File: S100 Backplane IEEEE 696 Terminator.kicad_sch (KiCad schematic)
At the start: 30 parts, among them IC1 7805, IC2 LM4250, P2 BUS_IN_1, P3 BUS_IN_2, Q1 2N3906, Q2 2N3904, Q3 TIP29, Q4 TIP30

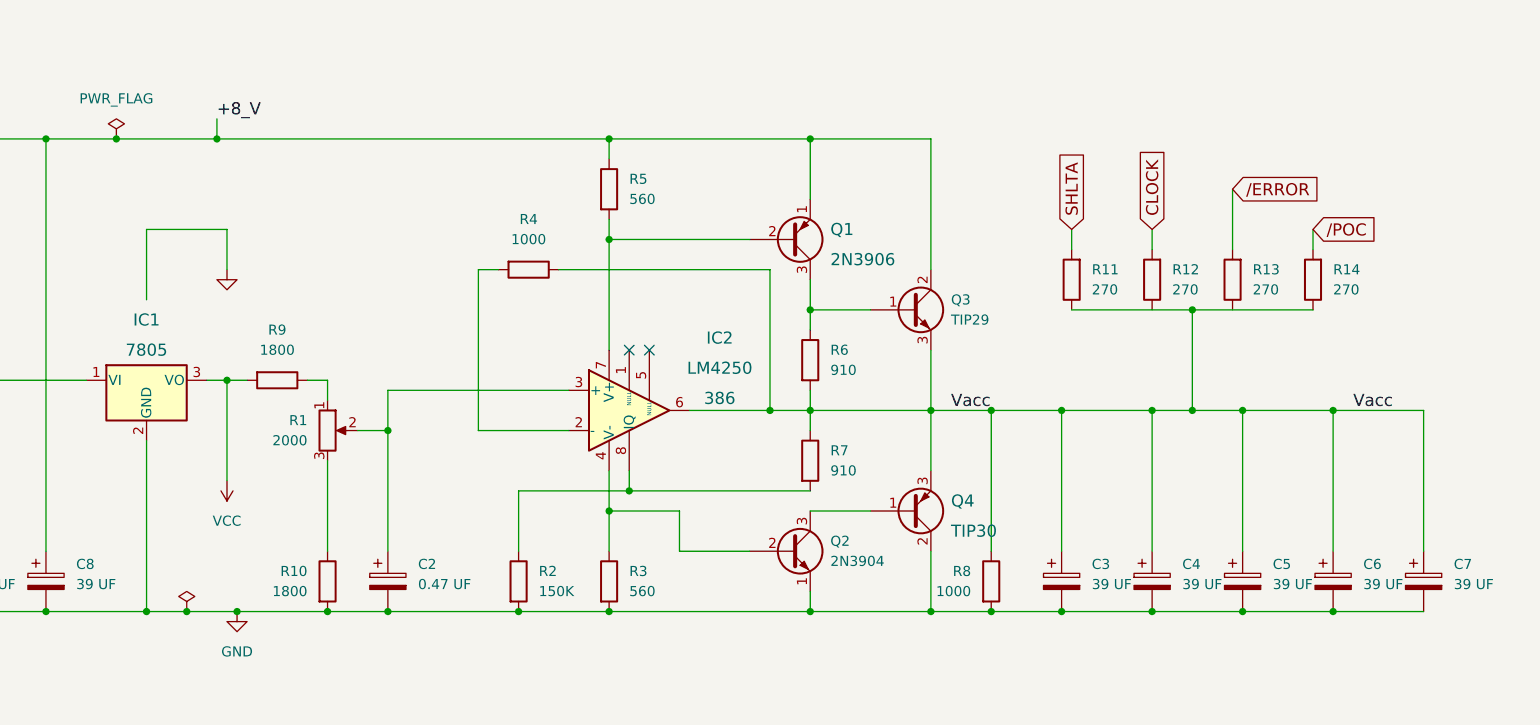
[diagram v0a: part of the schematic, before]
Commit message: Fix minor problem.
Signed-off-by: John Bradley <flypie@rocketmail.com>
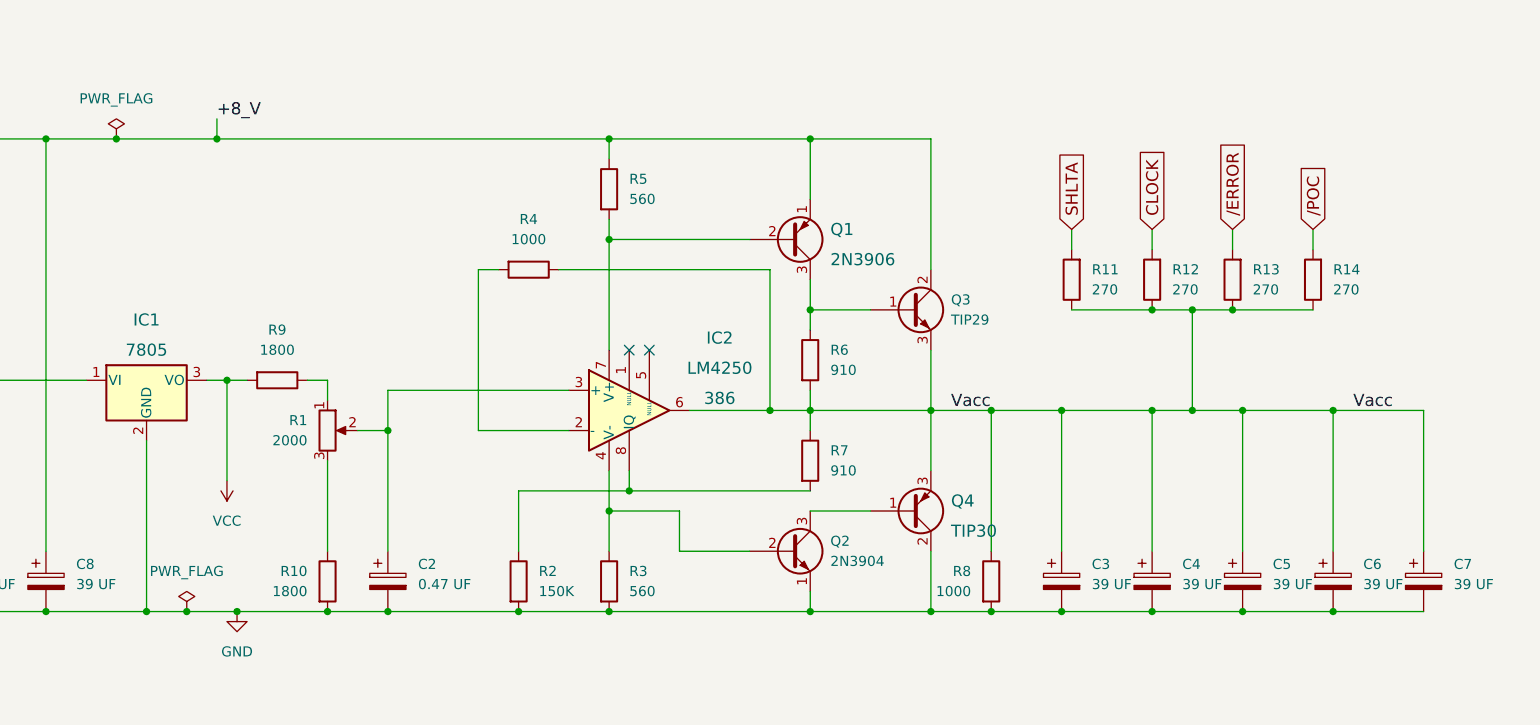
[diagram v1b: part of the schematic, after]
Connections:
- net Vacc: now also R12.1, R13.1
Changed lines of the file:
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@@
   (junction (at 226.06 92.71) (diameter 0) (color 0 0 0 0)
   )
+  (junction (at 237.49 54.61) (diameter 0) (color 0 0 0 0)
+  )
   (junction (at 194.31 33.02) (diameter 0) (color 0 0 0 0)
   )
@@
   )
   (junction (at 171.45 77.47) (diameter 0) (color 0 0 0 0)
+  )
+  (junction (at 247.65 54.61) (diameter 0) (color 0 0 0 0)
   )
   (junction (at 217.17 67.31) (diameter 0) (color 0 0 0 0)
@@
     (stroke (width 0) (type default) (color 0 0 0 0))
   )
-  (wire (pts (xy 110.49 53.34) (xy 110.49 44.45))
-    (stroke (width 0) (type default) (color 0 0 0 0))
-  )
   (wire (pts (xy 33.02 138.43) (xy 35.56 138.43))
     (stroke (width 0) (type default) (color 0 0 0 0))
@@
     (stroke (width 0) (type default) (color 0 0 0 0))
   )
-  (wire (pts (xy 120.65 44.45) (xy 120.65 49.53))
-    (stroke (width 0) (type default) (color 0 0 0 0))
-  )
   (wire (pts (xy 133.35 63.5) (xy 133.35 66.04))
     (stroke (width 0) (type default) (color 0 0 0 0))
@@
     (stroke (width 0) (type default) (color 0 0 0 0))
   )
-  (wire (pts (xy 227.33 54.61) (xy 242.57 54.61))
+  (wire (pts (xy 227.33 54.61) (xy 237.49 54.61))
     (stroke (width 0) (type default) (color 0 0 0 0))
   )
@@
     (stroke (width 0) (type default) (color 0 0 0 0))
   )
-  (wire (pts (xy 247.65 46.99) (xy 247.65 39.37))
+  (wire (pts (xy 247.65 46.99) (xy 247.65 44.45))
     (stroke (width 0) (type default) (color 0 0 0 0))
   )
@@
     (stroke (width 0) (type default) (color 0 0 0 0))
   )
-  (wire (pts (xy 110.49 44.45) (xy 120.65 44.45))
-    (stroke (width 0) (type default) (color 0 0 0 0))
-  )
   (wire (pts (xy 217.17 92.71) (xy 226.06 92.71))
     (stroke (width 0) (type default) (color 0 0 0 0))
@@
     (stroke (width 0) (type default) (color 0 0 0 0))
   )
-  (wire (pts (xy 242.57 54.61) (xy 257.81 54.61))
+  (wire (pts (xy 242.57 54.61) (xy 247.65 54.61))
+    (stroke (width 0) (type default) (color 0 0 0 0))
+  )
+  (wire (pts (xy 247.65 54.61) (xy 257.81 54.61))
     (stroke (width 0) (type default) (color 0 0 0 0))
   )
@@
   )
   (wire (pts (xy 48.26 57.15) (xy 50.8 57.15))
+    (stroke (width 0) (type default) (color 0 0 0 0))
+  )
+  (wire (pts (xy 237.49 54.61) (xy 242.57 54.61))
     (stroke (width 0) (type default) (color 0 0 0 0))
   )
@@
     )
   )
-  (global_label "/POC" (shape input) (at 257.81 44.45 0) (fields_autoplaced)
-    (effects (font (size 1.524 1.524)) (justify left))
-    (property "Intersheet References" "${INTERSHEET_REFS}" (id 0) (at 266.84 44.3548 0)
+  (global_label "/POC" (shape input) (at 257.81 44.45 90) (fields_autoplaced)
+    (effects (font (size 1.524 1.524)) (justify left))
+    (property "Intersheet References" "${INTERSHEET_REFS}" (id 0) (at 257.7148 35.42 90)
       (effects (font (size 1.524 1.524)) (justify left))
     )
@@
     )
   )
-  (global_label "{slash}ERROR" (shape input) (at 247.65 39.37 0) (fields_autoplaced)
-    (effects (font (size 1.524 1.524)) (justify left))
-    (property "Intersheet References" "${INTERSHEET_REFS}" (id 0) (at 259.5829 39.2748 0)
+  (global_label "{slash}ERROR" (shape input) (at 247.65 44.45 90) (fields_autoplaced)
+    (effects (font (size 1.524 1.524)) (justify left))
+    (property "Intersheet References" "${INTERSHEET_REFS}" (id 0) (at 247.5548 32.5171 90)
       (effects (font (size 1.524 1.524)) (justify left))
     )
@@
     (pin "2")
   )
-  (symbol (lib_id "power:GND") (at 120.65 49.53 0) (unit 1)
-    (in_bom yes) (on_board yes) (fields_autoplaced)
-    (property "Reference" "#PWR04" (id 0) (at 120.65 49.53 0)
-      (effects (font (size 0.762 0.762)) hide)
-    )
-    (property "Value" "GND" (id 1) (at 120.65 51.308 0)
-      (effects (font (size 0.762 0.762)) hide)
-    )
-    (property "Footprint" "" (id 2) (at 120.65 49.53 0)
-      (effects (font (size 1.27 1.27)) hide)
-    )
-    (property "Datasheet" "" (id 3) (at 120.65 49.53 0)
-      (effects (font (size 1.27 1.27)) hide)
-    )
-    (pin "1")
-  )
   (symbol (lib_id "power:GND") (at 50.8 74.93 90) (unit 1)
     (in_bom yes) (on_board yes)
@@
       (effects (font (size 1.27 1.27)) hide)
     )
-    (property "Value" "" (id 1) (at 115.57 87.63 0))
+    (property "Value" "PWR_FLAG" (id 1) (at 115.57 87.63 0))
     (property "Footprint" "" (id 2) (at 115.57 92.71 0)
       (effects (font (size 1.27 1.27)) hide)
@@
       (reference "#FLG0102") (unit 1) (value "PWR_FLAG") (footprint "")
     )
-    (path "/00000000-0000-0000-0000-00004c3a0bfb"
-      (reference "#PWR04") (unit 1) (value "GND") (footprint "")
-    )
     (path "/1259bcd7-9588-482a-b334-dd57b7af1608"
